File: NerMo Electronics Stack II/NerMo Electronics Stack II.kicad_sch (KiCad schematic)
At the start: 1 part, among them J2 Conn_02x06_Odd_Even

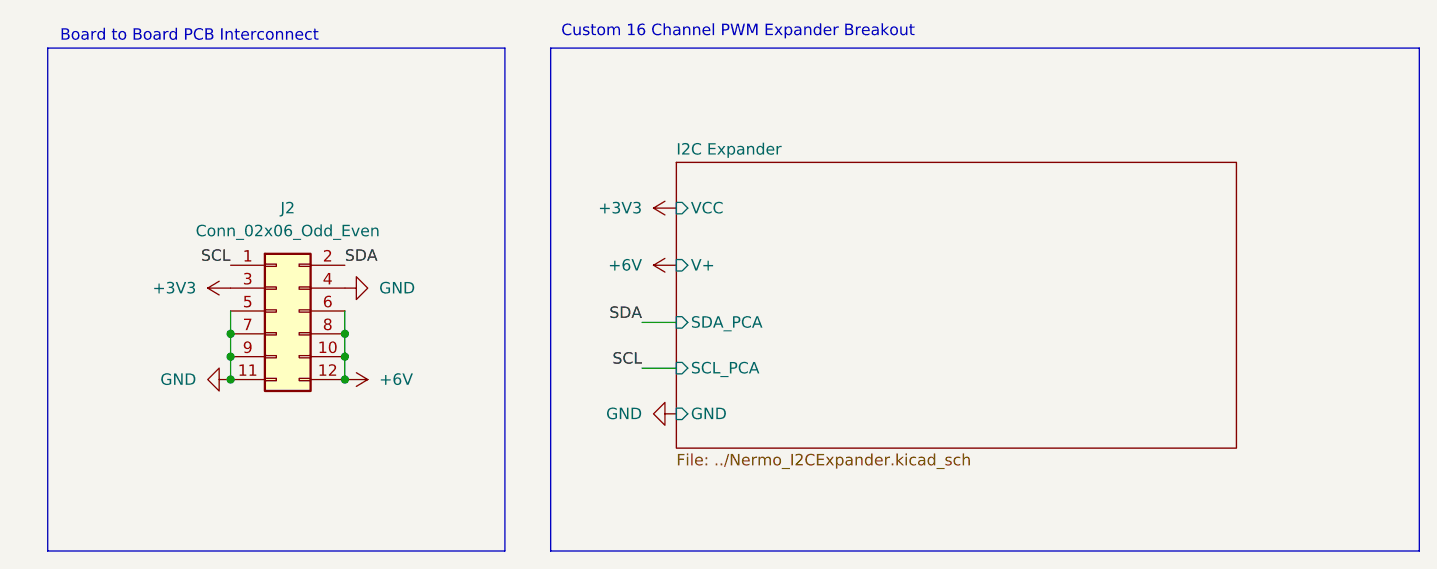
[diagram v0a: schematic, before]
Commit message: fix: fixed breakout interconnect pinout
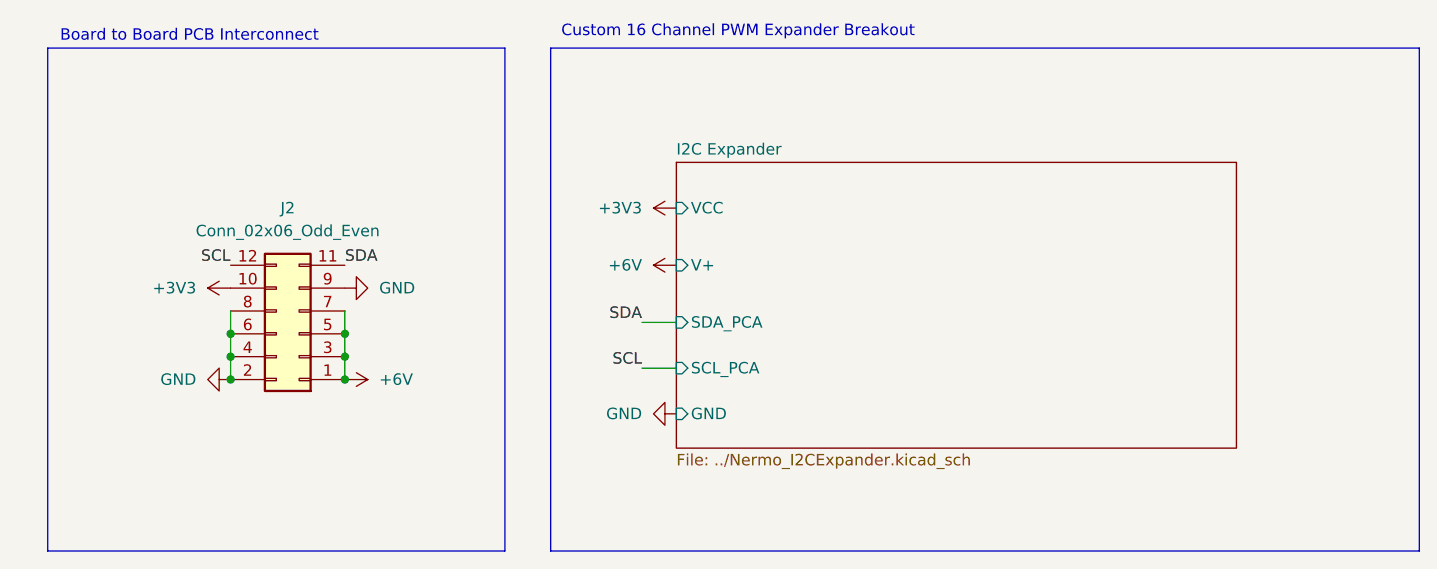
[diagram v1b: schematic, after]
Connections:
- net +3V3: now also J2.10 (Pin_10); no longer J2.3 (Pin_3)
- net +6V: now also J2.1 (Pin_1), J2.3 (Pin_3), J2.5 (Pin_5), J2.7 (Pin_7); no longer J2.10 (Pin_10), J2.12 (Pin_12), J2.6 (Pin_6), J2.8 (Pin_8)
- net GND: now also J2.2 (Pin_2), J2.6 (Pin_6), J2.8 (Pin_8); no longer J2.11 (Pin_11), J2.5 (Pin_5), J2.7 (Pin_7)
- net SCL: now also J2.12 (Pin_12); no longer J2.1 (Pin_1)
- net SDA: now also J2.11 (Pin_11); no longer J2.2 (Pin_2)
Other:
- moved on the sheet: J2
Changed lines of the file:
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@@
+	)
+	(junction
+		(at 82.55 102.87)
+		(diameter 0)
+		(color 0 0 0 0)
+	)
+	(junction
+		(at 69.85 107.95)
+		(diameter 0)
+		(color 0 0 0 0)
+	)
+	(junction
+		(at 82.55 107.95)
+		(diameter 0)
+		(color 0 0 0 0)
+	)
+	(junction
+		(at 82.55 105.41)
+		(diameter 0)
+		(color 0 0 0 0)
+	)
+	(junction
+		(at 69.85 105.41)
+		(diameter 0)
+		(color 0 0 0 0)
 	)
 	(junction
@@
 		(color 0 0 0 0)
 	)
-	(junction
-		(at 69.85 105.41)
-		(diameter 0)
-		(color 0 0 0 0)
-	)
-	(junction
-		(at 82.55 107.95)
-		(diameter 0)
-		(color 0 0 0 0)
-	)
-	(junction
-		(at 69.85 107.95)
-		(diameter 0)
-		(color 0 0 0 0)
-	)
-	(junction
-		(at 82.55 102.87)
-		(diameter 0)
-		(color 0 0 0 0)
-	)
-	(junction
-		(at 82.55 105.41)
-		(diameter 0)
-		(color 0 0 0 0)
+	(wire
+		(pts
+			(xy 82.55 102.87) (xy 82.55 105.41)
+		)
+		(stroke
+			(width 0)
+			(type default)
+		)
 	)
 	(wire
@@
 	(wire
 		(pts
-			(xy 69.85 102.87) (xy 69.85 100.33)
+			(xy 69.85 102.87) (xy 69.85 105.41)
+		)
+		(stroke
+			(width 0)
+			(type default)
+		)
+	)
+	(wire
+		(pts
+			(xy 82.55 105.41) (xy 82.55 107.95)
 		)
 		(stroke
@@
 	(wire
 		(pts
-			(xy 82.55 102.87) (xy 82.55 105.41)
-		)
-		(stroke
-			(width 0)
-			(type default)
-		)
-	)
-	(wire
-		(pts
-			(xy 69.85 102.87) (xy 69.85 105.41)
-		)
-		(stroke
-			(width 0)
-			(type default)
-		)
-	)
-	(wire
-		(pts
-			(xy 69.85 107.95) (xy 69.85 105.41)
-		)
-		(stroke
-			(width 0)
-			(type default)
-		)
-	)
-	(wire
-		(pts
-			(xy 82.55 105.41) (xy 82.55 107.95)
+			(xy 69.85 100.33) (xy 69.85 102.87)
+		)
+		(stroke
+			(width 0)
+			(type default)
+		)
+	)
+	(wire
+		(pts
+			(xy 69.85 105.41) (xy 69.85 107.95)
 		)
 		(stroke
@@
 	(symbol
 		(lib_id "Connector_Generic:Conn_02x06_Odd_Even")
-		(at 74.93 100.33 0)
+		(at 77.47 102.87 180)
 		(unit 1)
 		(exclude_from_sim no)
@@
 		(on_board yes)
 		(dnp no)
-		(fields_autoplaced yes)
 		(property "Reference" "J2"
 			(at 76.2 88.9 0)
@@
 		)
 		(property "Footprint" "Connector_PinHeader_1.27mm:PinHeader_2x06_P1.27mm_Vertical"
-			(at 74.93 100.33 0)
+			(at 77.47 102.87 0)
 			(effects
 				(font
@@
 		)
 		(property "Datasheet" "~"
-			(at 74.93 100.33 0)
+			(at 77.47 102.87 0)
 			(effects
 				(font
@@
 		)
 		(property "Description" "Generic connector, double row, 02x06, odd/even pin numbering scheme (row 1 odd numbers, row 2 even numbers), script generated (kicad-library-utils/schlib/autogen/connector/)"
-			(at 74.93 100.33 0)
+			(at 77.47 102.87 0)
 			(effects
 				(font
@@
 		)
 		(instances
-			(project ""
+			(project "NerMo Electronics Stack II"
 				(path "/39dca41c-80f9-47b6-a9d6-5e39413b947c"
 					(reference "J2")
